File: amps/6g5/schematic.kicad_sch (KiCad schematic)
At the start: 97 parts, among them SW1 AC

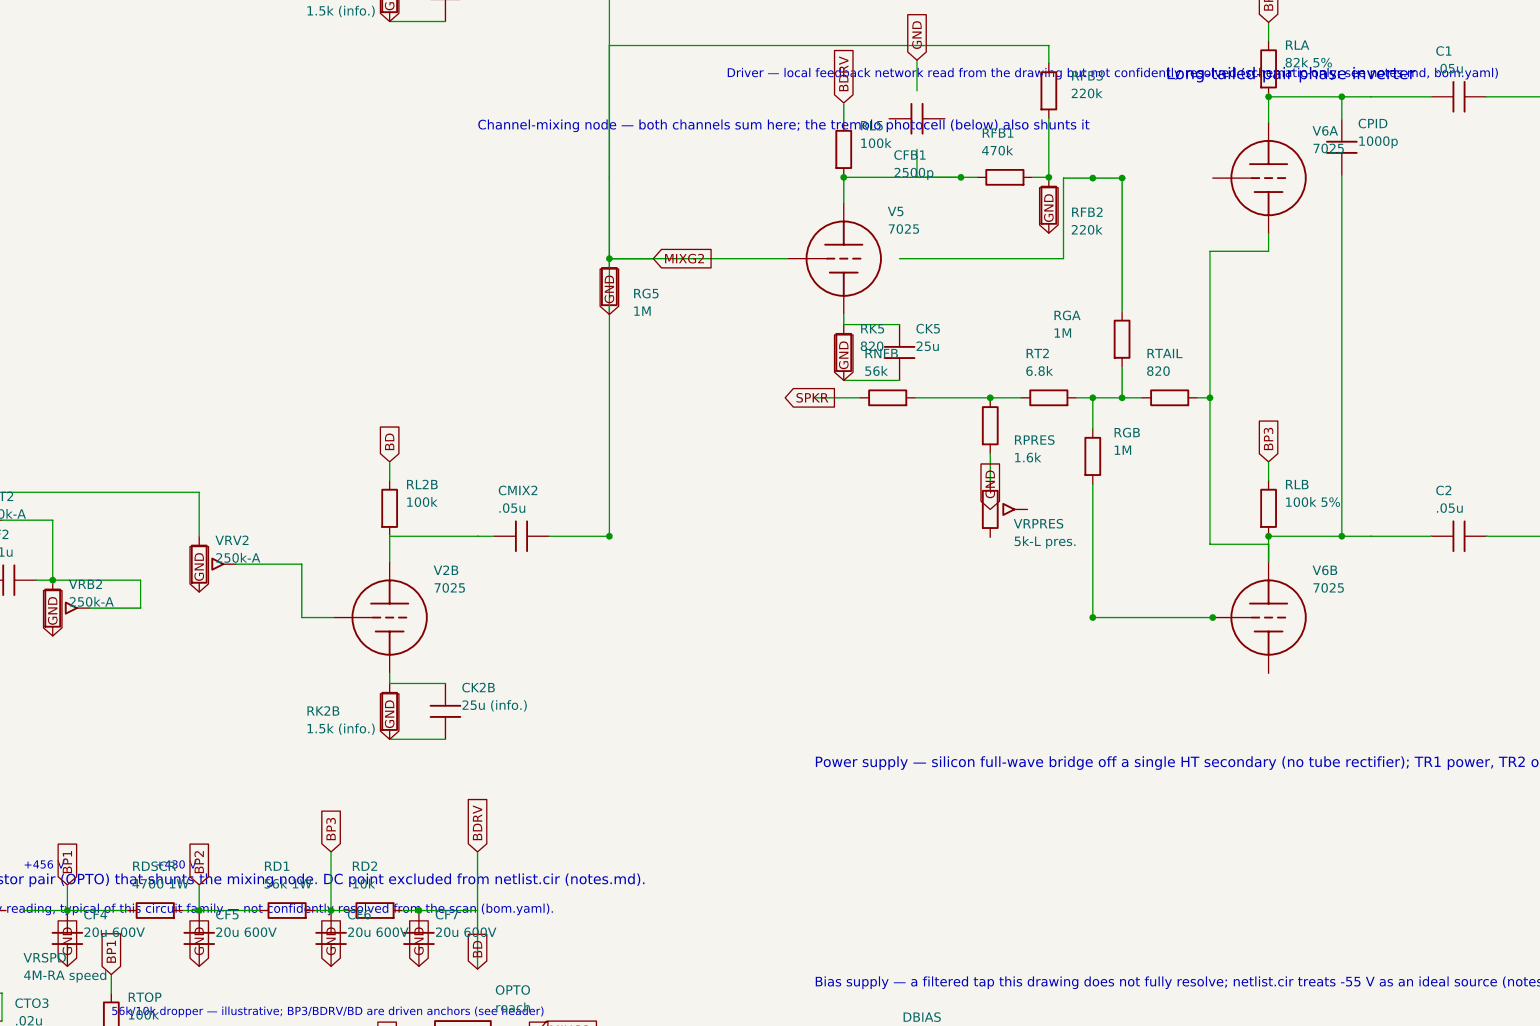
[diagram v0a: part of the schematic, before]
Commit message: Fix: one lettering convention per surface, engine-enforced; legend inside the viewBox
WS3 — layout pipeline + cross-surface value-consistency engine.

## One convention per surface (docs/lettering-conventions.md, new)

The same part stated its value in several notations at once. 5E3 C6 and 5D3 C6
rendered "5n" on the schematic, "0.005 µF · 600 V" in the parts list and
"0.005 µF" on the board. 5F6-A RD1 printed "4,700 Ω" beside neighbours printing
"15 kΩ". check_value_consistency proves the surfaces name the same QUANTITY; it
cannot see that they name it three ways. So each surface now has exactly one
convention and every one of them is gated:

* house units in bom.yaml/prose — engineering prefix with the mantissa 1…999,
  pF below 1000 pF and µF at and above it, no comma-grouped thousands. 19 values
  normalised (5E6-A, 5F6-A, 5F10, 6161, 6G2, 6G5, 6G6-B).
* schematic drafting shorthand — the unit letter is the SI prefix of the house
  unit, in the amp's declared idiom (meta.yaml conventions.notation: us|uk).
  British RKM/nanofarad practice on the Hiwatt and the 2204 is DECLARED, not
  normalised away; it is what those source drawings letter. Secondary ratings
  are space-separated fields with their own unit ("20u 600V"), never the era's
  dashed shorthand and never the house middot. 30 symbol values corrected across
  ten draw scripts.
* era sheet lettering — generated only, by era_pair(); documented cases and a
  corpus round-trip sweep in test_era_values.py, now 57 cases.

## Era-lettering fall-throughs closed

A value era_pair() refuses came back as the house string, and a house string can
be a whole sentence. Fixed at the source rather than per case:

* body_value() — a parenthetical GLOSS is never lettered on a component body.
  "selenium (silicon diode in modern builds)" was lettered in full on the 5E4-A
  and ran off the left edge of the page.
* twin cans letter as the era sheets did: 25 µF + 25 µF -> "25/25MFD".
* a repeat count is not a rating: "(×2)" com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
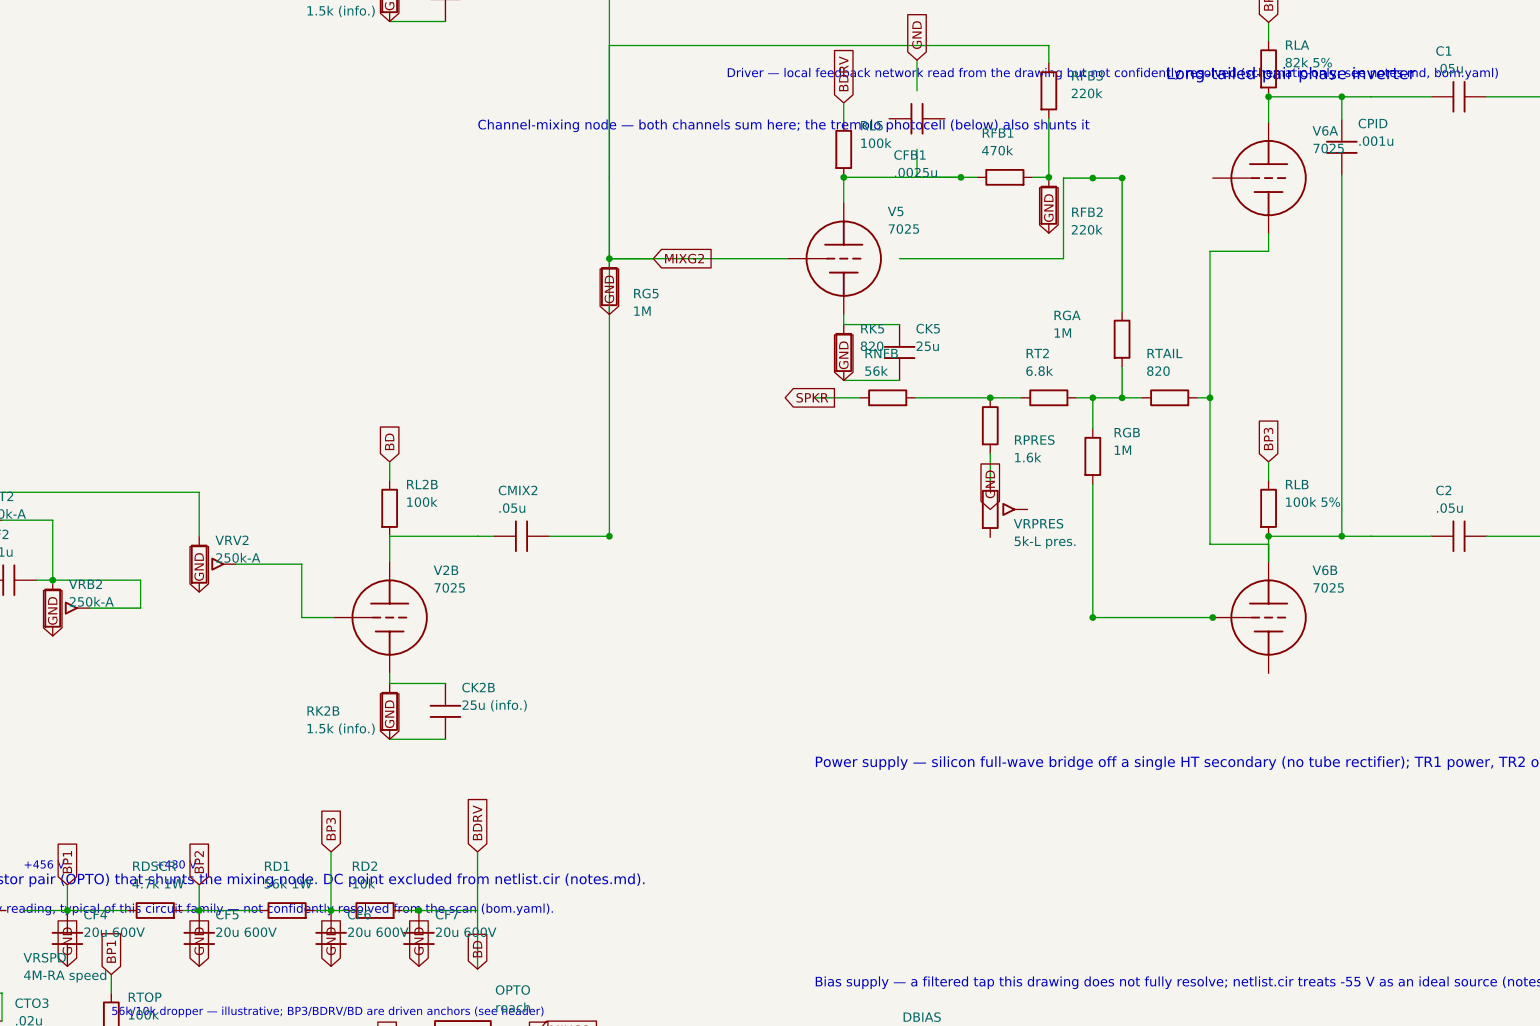
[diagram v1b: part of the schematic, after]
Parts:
- CFB1: value 2500p -> .0025u
- CPID: value 1000p -> .001u
- RDSCR: value 4700 1W -> 4.7k 1W
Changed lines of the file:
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@@
     (in_bom yes) (on_board yes)
     (property "Reference" "CFB1" (at 206.8 96.9 270) (effects (font (size 1.27 1.27)) (justify left)))
-    (property "Value" "2500p" (at 206.8 99.3 270) (effects (font (size 1.27 1.27)) (justify left))))
+    (property "Value" ".0025u" (at 206.8 99.3 270) (effects (font (size 1.27 1.27)) (justify left))))
   (wire (pts (xy 210 96.09) (xy 210 99.9))
     (stroke (width 0) (type default)))
@@
     (in_bom yes) (on_board yes)
     (property "Reference" "CPID" (at 270.2 92.6 0) (effects (font (size 1.27 1.27)) (justify left)))
-    (property "Value" "1000p" (at 270.2 95 0) (effects (font (size 1.27 1.27)) (justify left))))
+    (property "Value" ".001u" (at 270.2 95 0) (effects (font (size 1.27 1.27)) (justify left))))
   (wire (pts (xy 268 99.61) (xy 268 148.9))
     (stroke (width 0) (type default)))
@@
     (in_bom yes) (on_board yes)
     (property "Reference" "RDSCR" (at 102.8 194 270) (effects (font (size 1.27 1.27)) (justify left)))
-    (property "Value" "4700 1W" (at 102.8 196.4 270) (effects (font (size 1.27 1.27)) (justify left))))
+    (property "Value" "4.7k 1W" (at 102.8 196.4 270) (effects (font (size 1.27 1.27)) (justify left))))
   (wire (pts (xy 100 200) (xy 102.19 200))
     (stroke (width 0) (type default)))

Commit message: Update: regenerate every drawing the four merged units changed
The four parallel units all rewrote generators, so their committed artifacts
were each generated against only their own third of the merged pipeline. Every
schematic, both layout styles, the social cards and the manifest are rebuilt
here from the merged sources, so what ships is what the merged generators draw.

One integration fault the rebuild exposed, invisible to any single unit:

- 5E5-A: the note explaining that the Presence wiper and the 100k feedback
  resistor land on V3A's GRID (not its cathode, as on the 5F4) was added as a
  hand-placed `s.text()` at a coordinate chosen before the sheet gained a
  reserved notes band. Merged, it printed through the -32V bias label. Moved to
  `note()`, which wraps prose into that band — the exact failure mode the band
  was built to end.

Three conflicts resolved against docs/lettering-conventions.md rather than by
picking a side, since two units had corrected the same lines for different
reasons:

- 5E5-A tone/feedback caps take the corrected designators (C7, C8, C9, RNF —
  `C_tr1`/`C_NFB` were generator identifiers that had leaked onto a published
  board) with the house-derived lettering (`.01u 400V`, `500p`, `.1u 200V`).
  Dropping the working voltage or writing `.0005u` would have lost a rating the
  source prints and re-broken the pF/µF decade rule.
- 5D3 C6 and 6G6-B's three cathode resistors take the SI-prefix form the
  convention binds (`.005u`, `2.7k`, `1.5k`), keeping the ground-flag direction
  fix and the removal of the second `gnd()` that shorted each cathode it biased.
- 5F6-A's bias supply keeps both 8 µF cans drawn — the second was previously a
  parenthetical claiming one of two was shown — at the coordinates that clear
  the title-block strip.

All gates green, including check_value_consistency at zero disagreements.

🤖 Generated with [Claude Code](https://claude.com/claude-code)

Co-Authored-By: Claude Fable 5 <noreply@anthropic.com>
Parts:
- OPTO: value roach -> optocoupler
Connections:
- net GND: now also VRPRES.3
- net at VRB2.1, VRB2.2 (W), VRT2.2 (W): no longer CF2.2
- net at VRB1.1, VRB1.2 (W), VRT1.2 (W): no longer CF1.2
- net at CTO1.2, VRSPD.3: no longer CTO3.1
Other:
- note removed: "6G5 — Brown Pro-style · Circuit Codex · CC-BY-SA 4.0 · redrawn from circuit facts"
- company: (none) -> Circuit Codex
- title: (none) -> 6G5 — Brown Pro-style

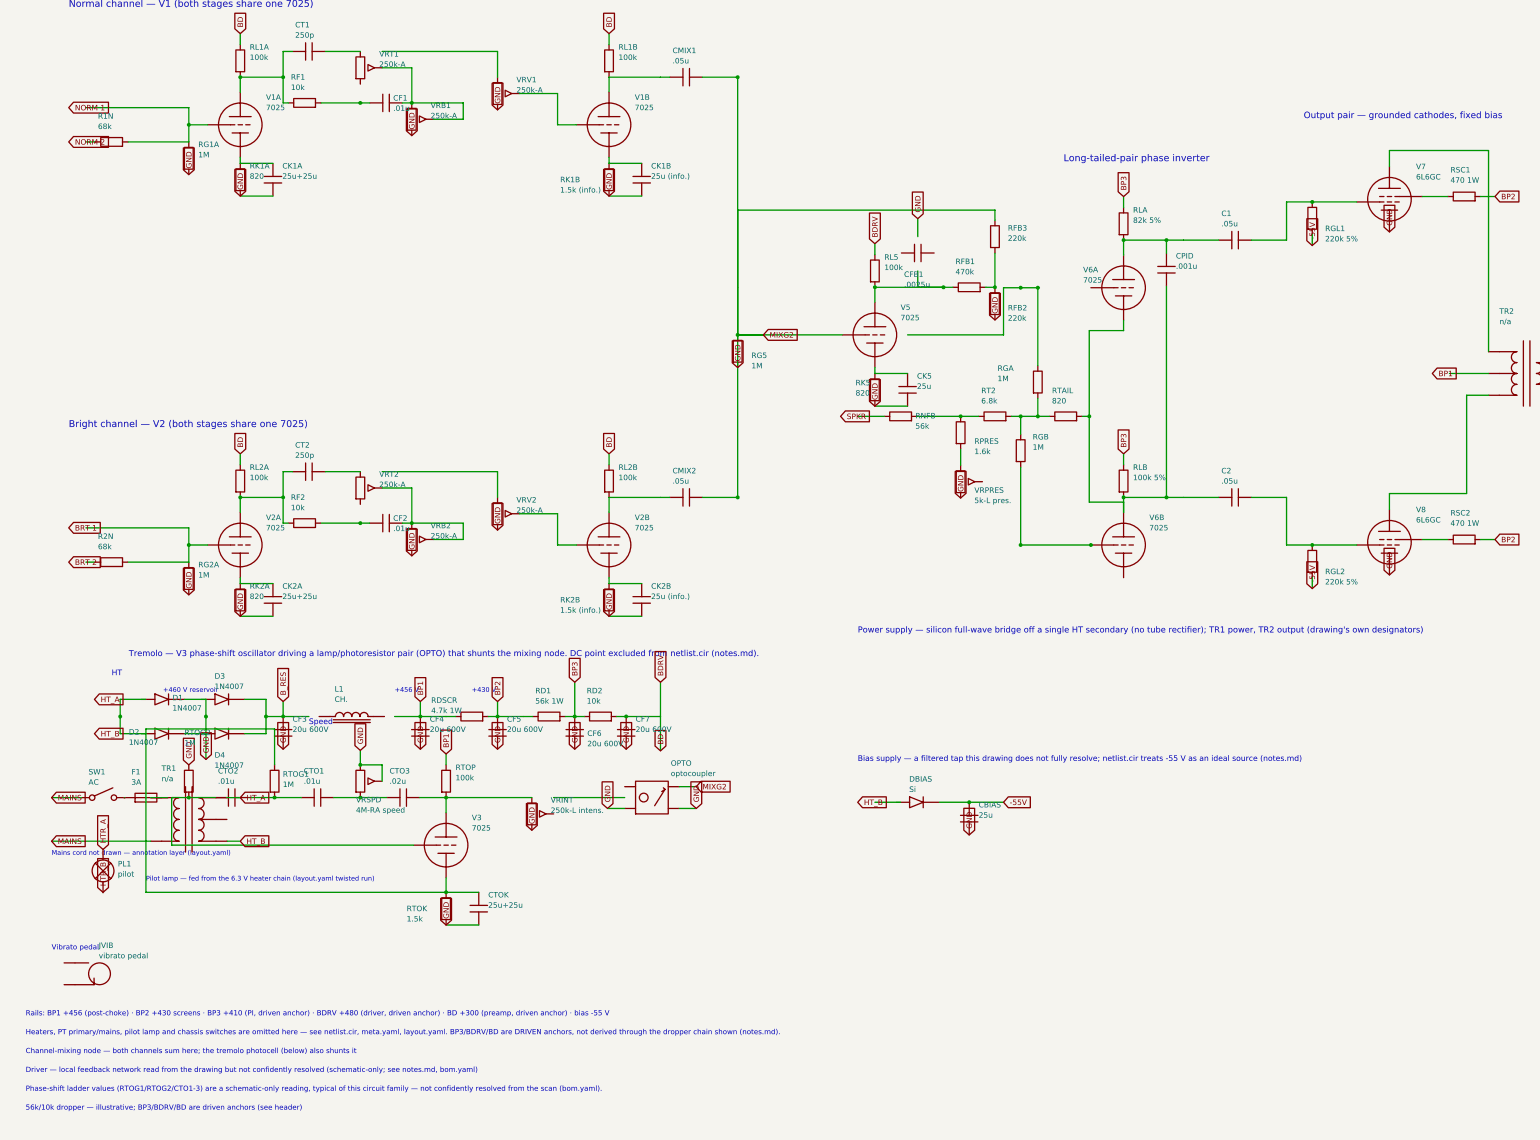
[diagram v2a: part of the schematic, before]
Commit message: Fix: label-wire abutments the gate cannot see, caught by reading pixels
Four sites from the closing visual pass, each a designator or value line
sitting on live wiring below gate sensitivity (wires are not a clash class,
and the old placement ruler under-read text width):

- 5F6-A: RB2's block, squeezed into the 2.5 mm channel beside C15, printed
  through its own resistor body and into C15b's designator. Authored anchor
  now letters it above the supply wire, between RB1's lettering and the -48V
  flag — the one clear pocket in that cramped bias block.
- 6G4: the Speed pot's "4M-RA speed" value line lay on the oscillator ladder
  wire and CTO2's pin; anchored clear (the true-ruler placer settles it left
  of the pot).
- 6G5: RNFB's vertical lettering straddled the NFB wire itself. Drawn
  directly instead of via series_h so the block can be pinned horizontal
  under the part. Also: the tremolo caption was a 175 mm single-sentence
  banner — wider than any clear band on the sheet, printing across the bias
  diodes wherever it was placed. It keeps its headline beside the V3 bottle;
  the mechanism sentence is a note, and notes live in the band.
- 1959: both volume pots' "1M vol" crossed the wiper wire and RM1/RM2's
  pins; anchored clear of the pot body (placer settles them left).

6G6-B's RK2B/CK2B crowding (the fourth verdict item) needed no draw-script
change: the renderer-metric placer from the previous commit already moves the
block clear of the tie wire.

🤖 Generated with [Claude Code](https://claude.com/claude-code)

Co-Authored-By: Claude Fable 5 <noreply@anthropic.com>
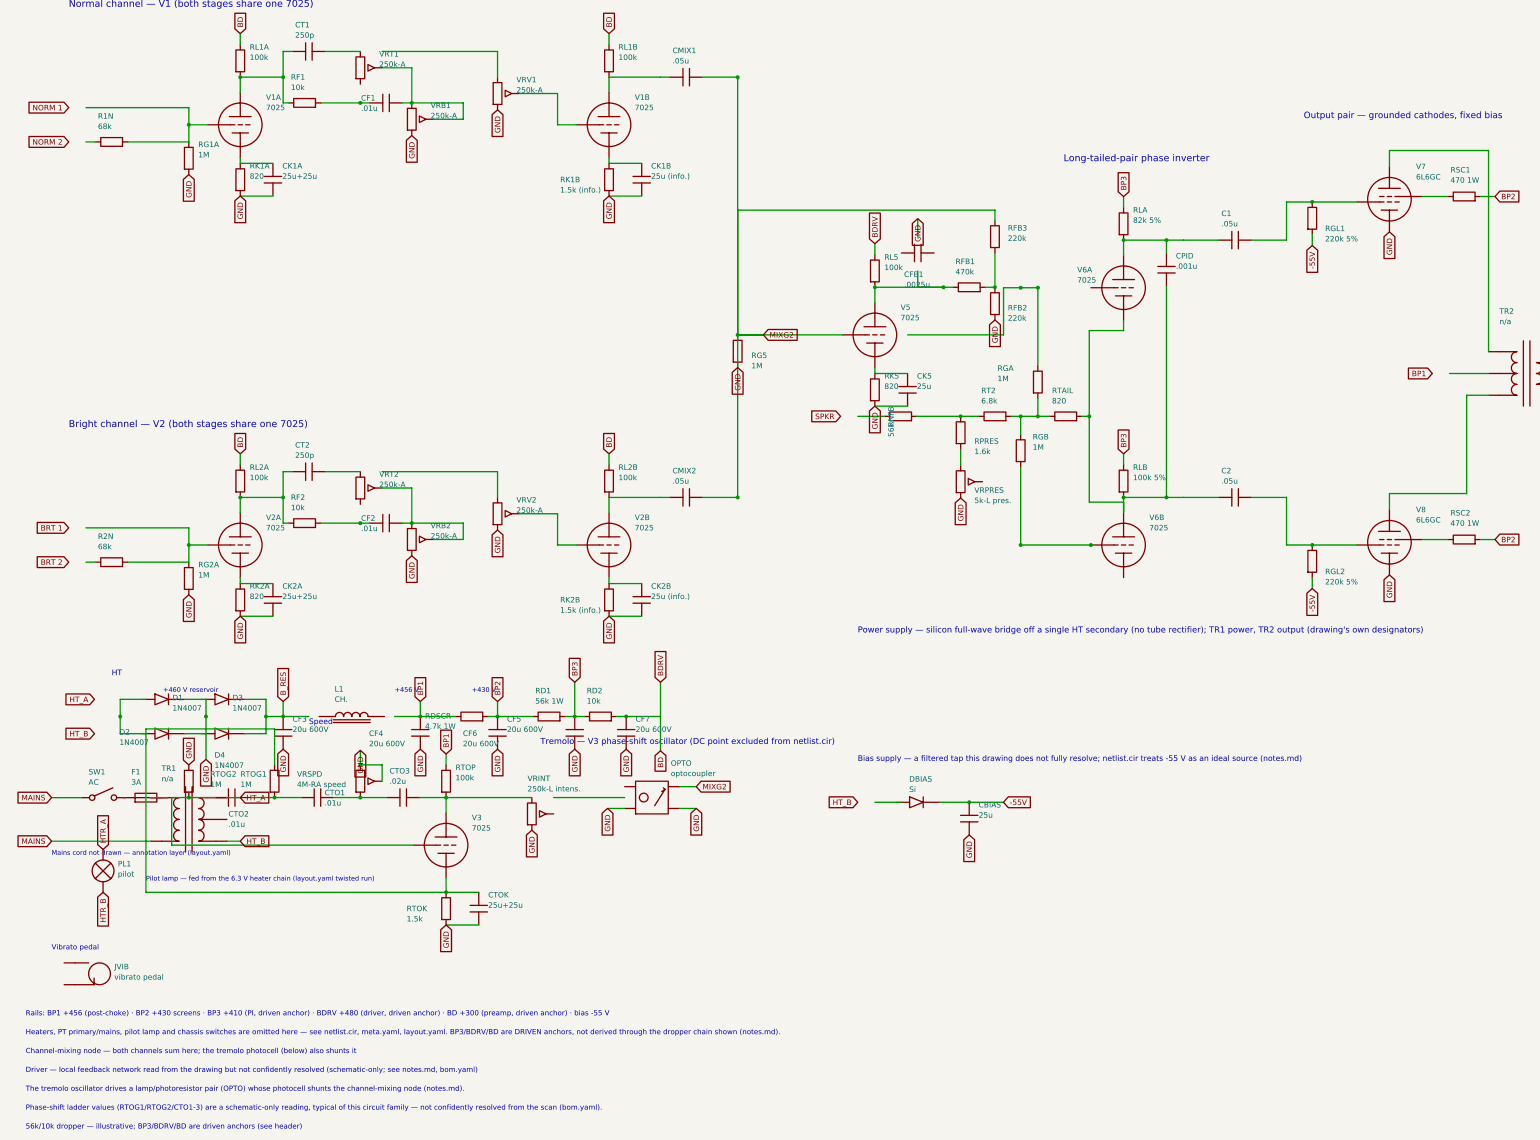
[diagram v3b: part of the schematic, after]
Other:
- note added: "The tremolo oscillator drives a lamp/photoresistor pair (OPTO) whose photocell shunts the channel-mixing node (notes.md)."
- note added: "Tremolo — V3 phase-shift oscillator (DC point excluded from netlist.cir)"
- note removed: "Tremolo — V3 phase-shift oscillator driving a lamp/photoresistor pair (OPTO) that shunts the mixing node. DC point excluded from netlist.cir (notes.md)."
